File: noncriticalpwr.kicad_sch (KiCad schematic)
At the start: 6 parts, among them J4 Power Conn

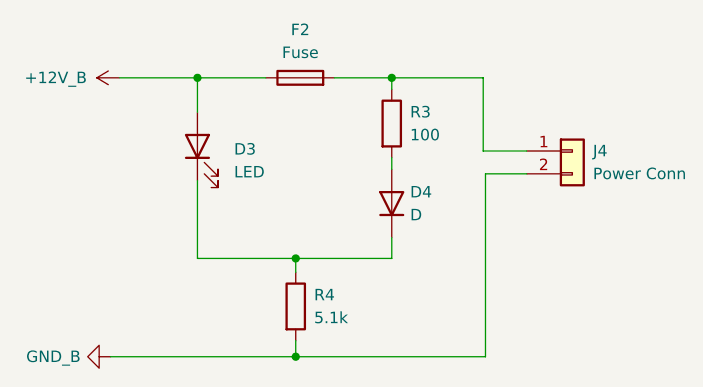
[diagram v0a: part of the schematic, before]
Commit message: removed LEDs
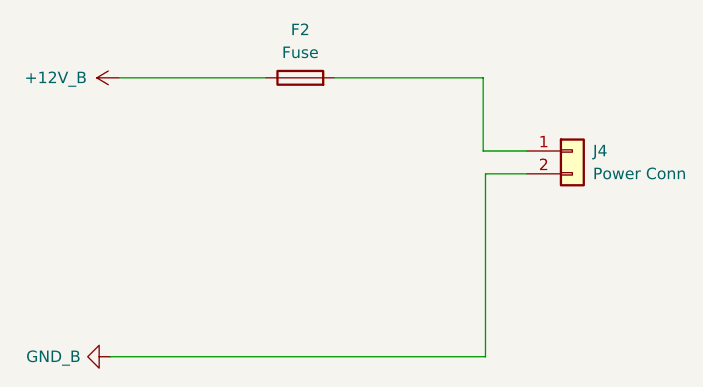
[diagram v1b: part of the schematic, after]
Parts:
- removed D3: LED, symbol Device:LED
- removed D4: D, symbol Device:D
- removed R3: 100, symbol Device:R
- removed R4: 5.1k, symbol Device:R

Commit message: finished schematic
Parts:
- added D10, D11, D12, D13, D14, D15, D16, D17, D18, D19, D8, D9: 20mA, LED_SMD:LED_0805_2012Metric, symbol Device:LED
- added F10, F11, F12, F13, F14, F15, F16, F17, F18, F19, F20: 10A, footprints:3588, symbol Device:Fuse
- added J1, J12, J13, J14, J15, J16, J17, J18, J19, J2, J20: NON CRIT OUT, footprints:Molex_Micro-Fit_3.0_43650-0215_1x02_P3.00mm_Vertical, symbol Connector_Generic:Conn_01x02
- added R10, R11, R12, R13, R14, R15, R16, R17, R18, R19, R8, R9: 505, Resistor_SMD:R_0805_2012Metric, symbol Device:R
- F2: value Fuse -> 10A
- J4: value Power Conn -> NON CRIT OUT
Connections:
- net at F2.2: now also J1.1 (Pin_1), R8.1; no longer J4.1 (Pin_1)
- net +12V_B renamed +12V_NON
- net +12V_NON: now also F10.1, F11.1, F12.1, F13.1, F14.1, F15.1, F16.1, F17.1, F18.1, F19.1, F20.1
- net GND_B renamed GND
- net GND: now also D10.1 (K), D11.1 (K), D12.1 (K), D13.1 (K), D14.1 (K), D15.1 (K), D16.1 (K), D17.1 (K), D18.1 (K), D19.1 (K), D8.1 (K), D9.1 (K), J1.2 (Pin_2), J12.2 (Pin_2), J13.2 (Pin_2), J14.2 (Pin_2), J15.2 (Pin_2), J16.2 (Pin_2), J17.2 (Pin_2), J18.2 (Pin_2), J19.2 (Pin_2), J2.2 (Pin_2), J20.2 (Pin_2)
- new net: F13.2, J13.1 (Pin_1), R12.1
- new net: D13.2 (A), R13.2
- new net: F14.2, J14.1 (Pin_1), R13.1
- new net: F20.2, J20.1 (Pin_1), R19.1
- new net: F12.2, J12.1 (Pin_1), R11.1
- new net: F10.2, J2.1 (Pin_1), R9.1
- new net: D19.2 (A), R19.2
- new net: D17.2 (A), R17.2
- new net: F19.2, J19.1 (Pin_1), R18.1
- new net: F15.2, J15.1 (Pin_1), R14.1
- new net: D15.2 (A), R15.2
- new net: D11.2 (A), R11.2
- new net: F16.2, J16.1 (Pin_1), R15.1
- new net: D8.2 (A), R8.2
- new net: F17.2, J17.1 (Pin_1), R16.1
- new net: D16.2 (A), R16.2
- new net: D14.2 (A), R14.2
- new net: D18.2 (A), R18.2
- new net: D12.2 (A), R12.2
- new net: F11.2, J4.1 (Pin_1), R10.1
- new net: D10.2 (A), R10.2
- new net: D9.2 (A), R9.2
- new net: F18.2, J18.1 (Pin_1), R17.1

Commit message: finished pcb
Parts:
- R10, R11, R12, R13, R14, R15, R16, R17, R18, R19, R8, R9: value 505 -> 1k
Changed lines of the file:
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@@
 			)
 		)
-		(property "Value" "505"
+		(property "Value" "1k"
 			(at 115.57 131.826 90)
 			(effects
@@
 			)
 		)
-		(property "Value" "505"
+		(property "Value" "1k"
 			(at 55.88 81.026 90)
 			(effects
@@
 			)
 		)
-		(property "Value" "505"
+		(property "Value" "1k"
 			(at 55.88 133.096 90)
 			(effects
@@
 			)
 		)
-		(property "Value" "505"
+		(property "Value" "1k"
 			(at 115.57 159.766 90)
 			(effects
@@
 			)
 		)
-		(property "Value" "505"
+		(property "Value" "1k"
 			(at 116.84 53.086 90)
 			(effects
@@
 			)
 		)
-		(property "Value" "505"
+		(property "Value" "1k"
 			(at 55.88 107.696 90)
 			(effects
@@
 			)
 		)
-		(property "Value" "505"
+		(property "Value" "1k"
 			(at 116.84 27.686 90)
 			(effects
@@
 			)
 		)
-		(property "Value" "505"
+		(property "Value" "1k"
 			(at 55.88 53.086 90)
 			(effects
@@
 			)
 		)
-		(property "Value" "505"
+		(property "Value" "1k"
 			(at 116.84 81.026 90)
 			(effects
@@
 			)
 		)
-		(property "Value" "505"
+		(property "Value" "1k"
 			(at 55.88 27.686 90)
 			(effects
@@
 			)
 		)
-		(property "Value" "505"
+		(property "Value" "1k"
 			(at 116.84 106.426 90)
 			(effects
@@
 			)
 		)
-		(property "Value" "505"
+		(property "Value" "1k"
 			(at 55.88 159.766 90)
 			(effects

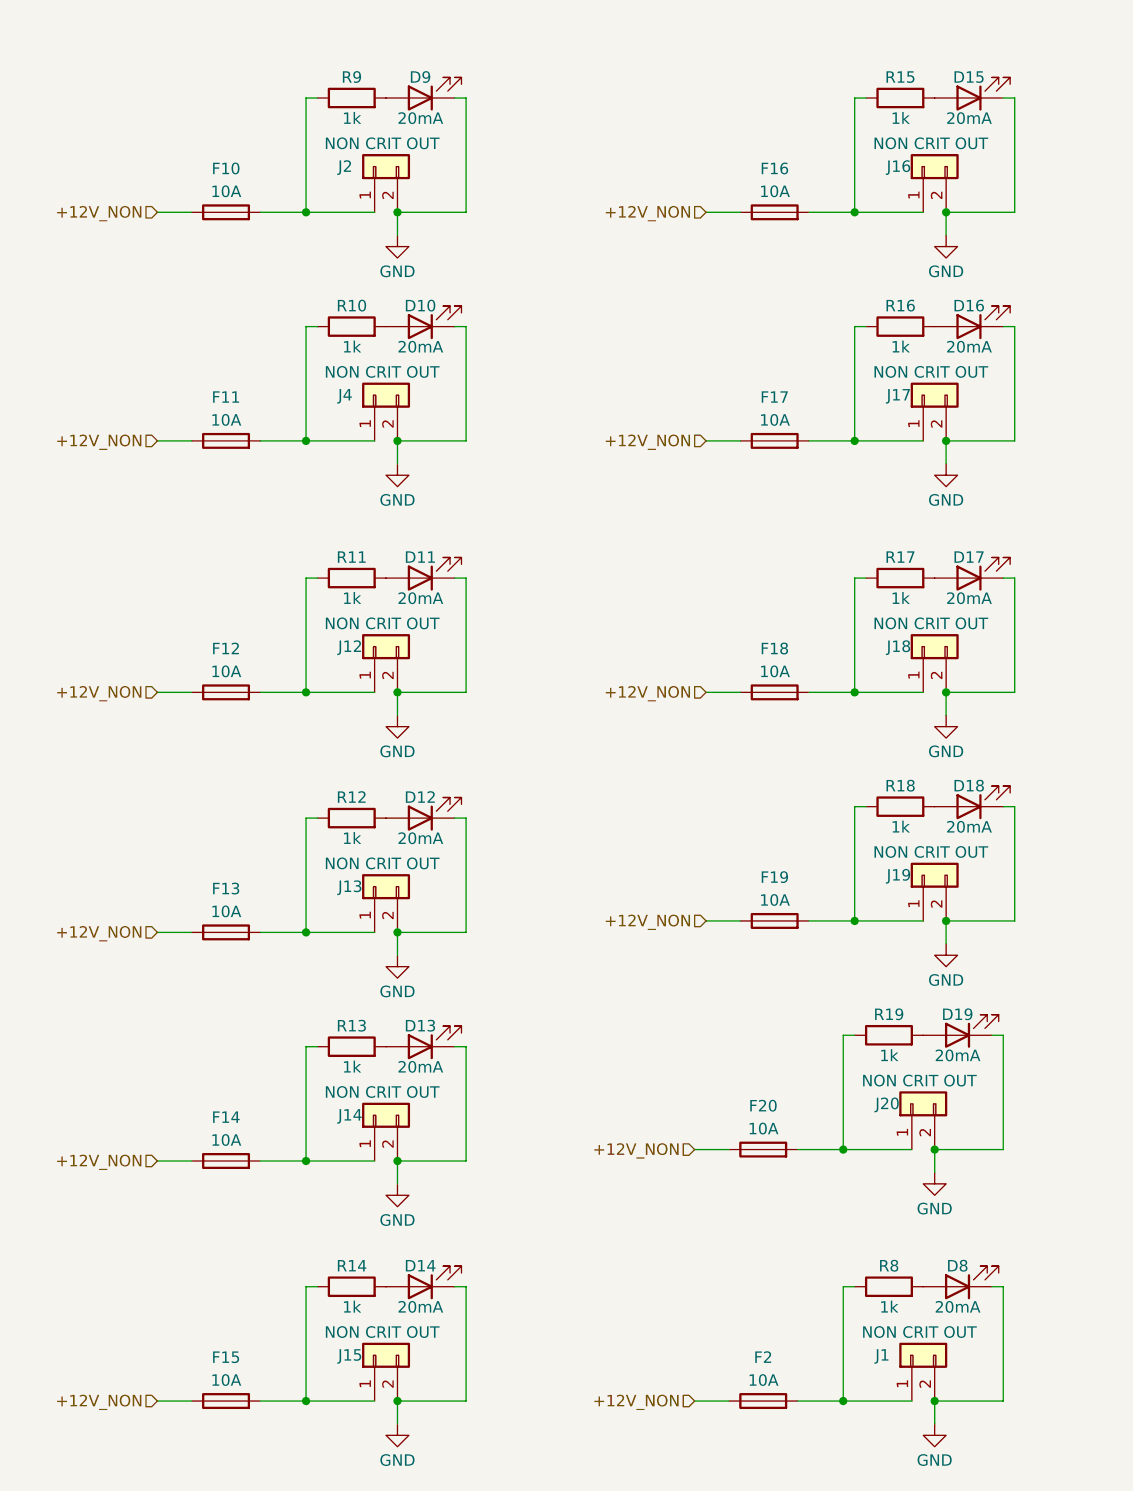
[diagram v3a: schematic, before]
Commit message: rearranged fuses on the back and and connectors on the front for improved waterproofing
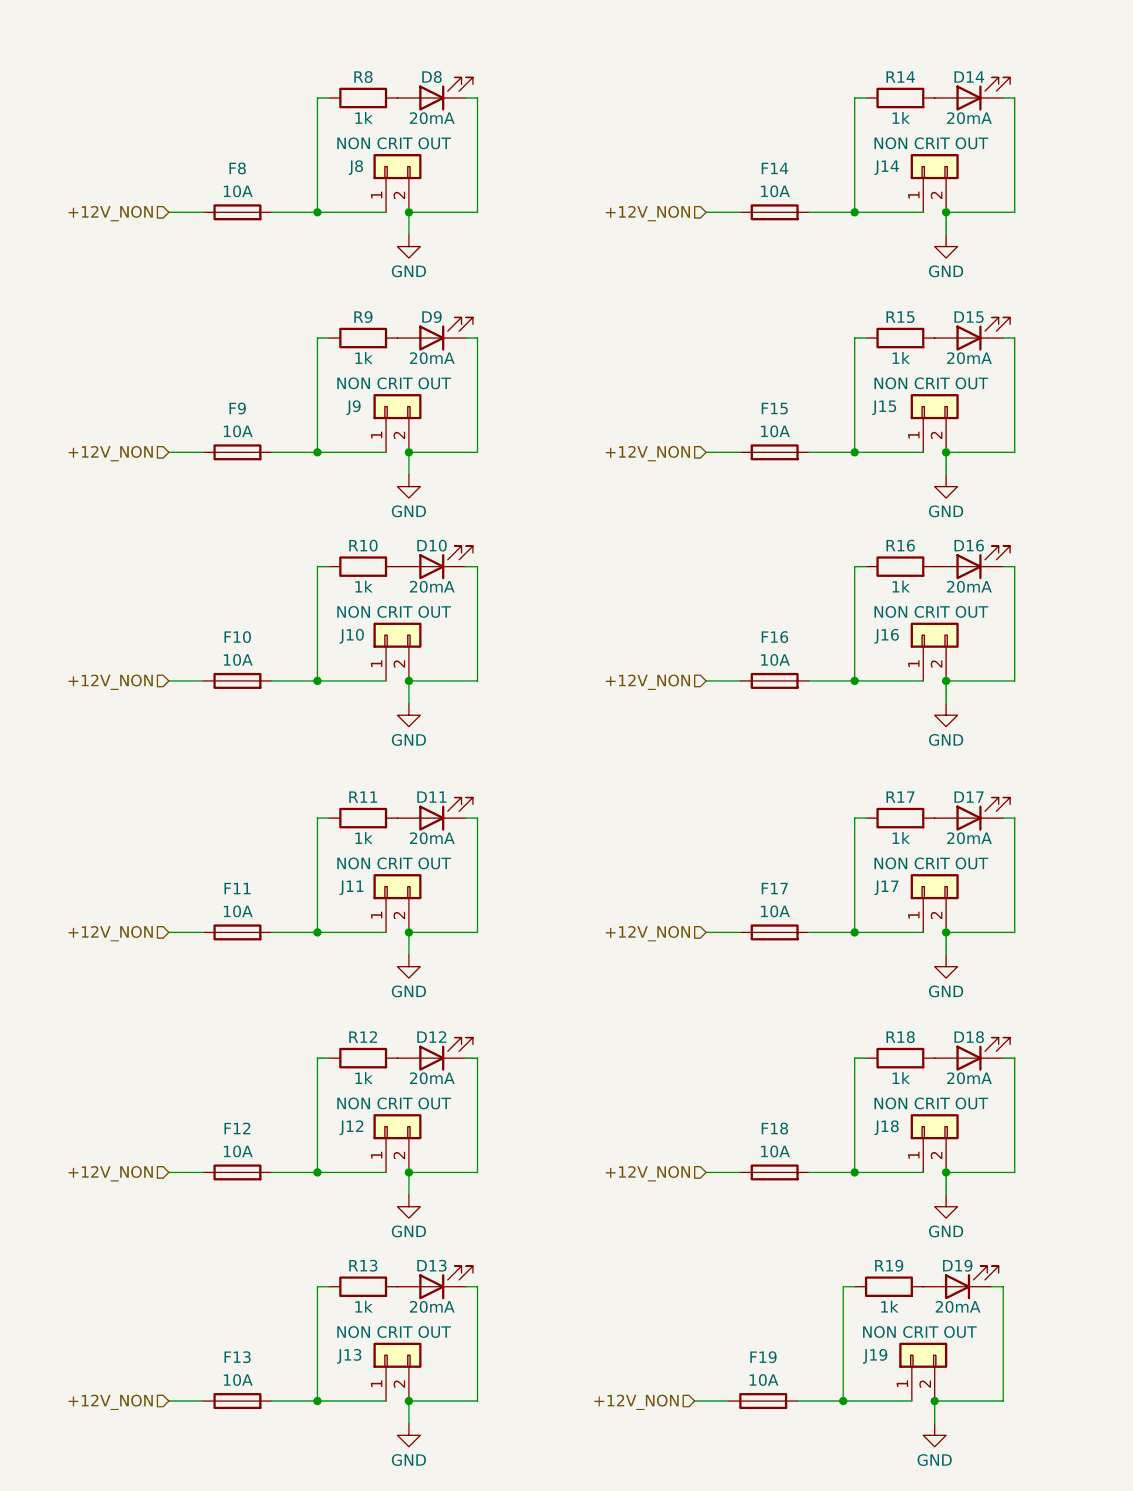
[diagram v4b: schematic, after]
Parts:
- renumbered F11 to F10, F12 to F11, F13 to F12, F14 to F13, F15 to F14, F16 to F15, F17 to F16, F18 to F17, F19 to F18, F20 to F19, F2 to F8, F10 to F9, J4 to J10, J12 to J11, J13 to J12, J14 to J13, J15 to J14, J16 to J15, J17 to J16, J18 to J17, J19 to J18, J20 to J19, J1 to J8, J2 to J9
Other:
- moved on the sheet: D10, D11, D12, D13, D14, D15, D16, D17, D18, D19, D8, D9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

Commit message: reoriented fuses horizontally to fit enclosure dimensions
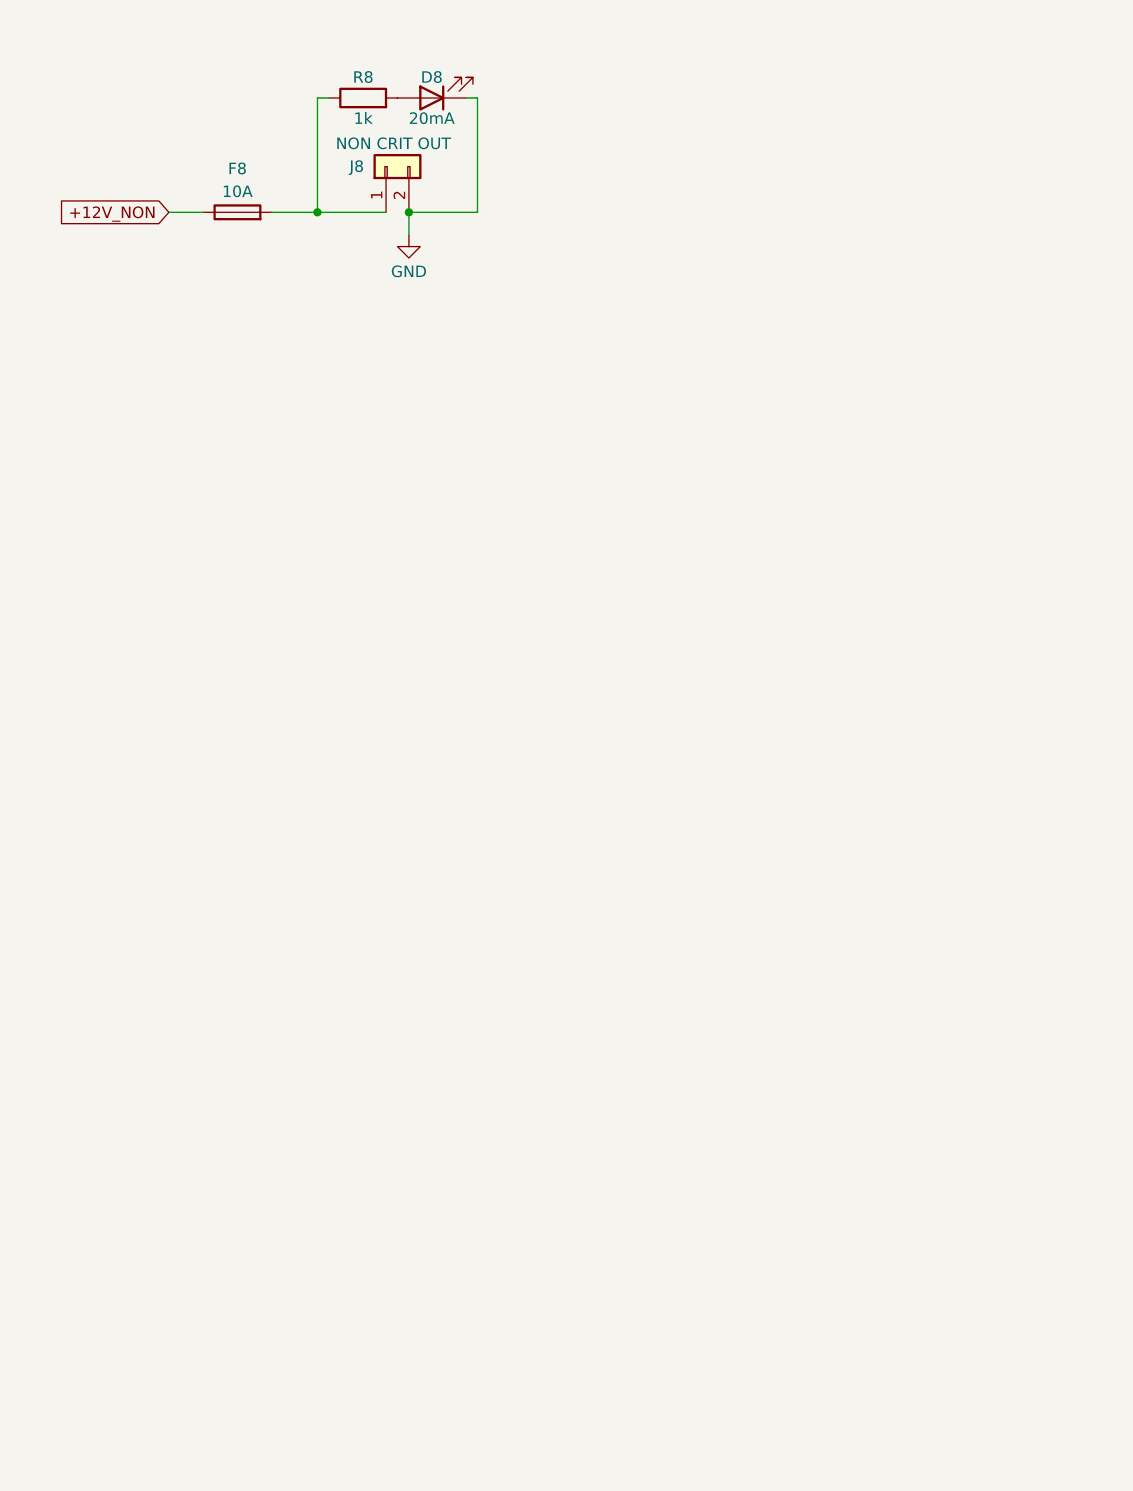
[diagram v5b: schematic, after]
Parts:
- removed D10, D11, D12, D13, D14, D15, D16, D17, D18, D19, D9: 20mA, LED_SMD:LED_0805_2012Metric, symbol Device:LED
- removed F10, F11, F12, F13, F14, F15, F16, F17, F18, F19, F9: 10A, footprints:3588, symbol Device:Fuse
- removed J10, J11, J12, J13, J14, J15, J16, J17, J18, J19, J9: NON CRIT OUT, footprints:Molex_Micro-Fit_3.0_43650-0215_1x02_P3.00mm_Vertical, symbol Connector_Generic:Conn_01x02
- removed R10, R11, R12, R13, R14, R15, R16, R17, R18, R19, R9: 1k, Resistor_SMD:R_0805_2012Metric, symbol Device:R

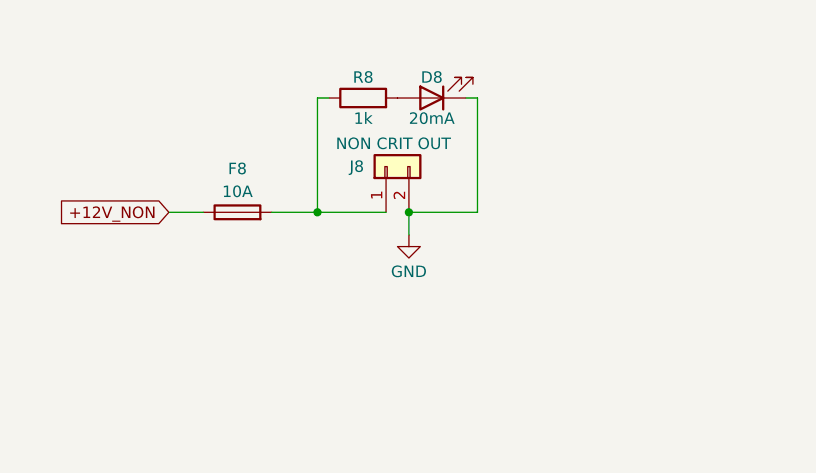
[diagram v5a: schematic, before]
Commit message: Added optoisolators to ensure LED indicators are powered by critical power and only turn on when the fuse blows. Fuses and resistors on the back for waterproofing.
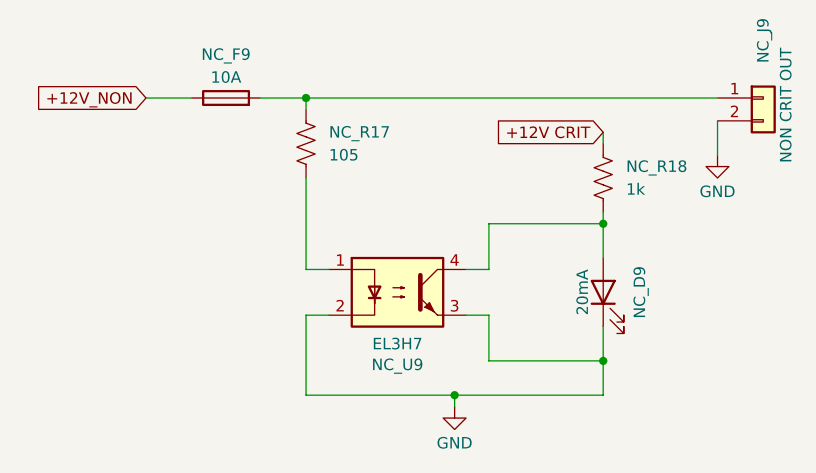
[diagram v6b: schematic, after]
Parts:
- removed D8: 20mA, LED_SMD:LED_0805_2012Metric, symbol Device:LED
- removed F8: 10A, footprints:3588, symbol Device:Fuse
- removed J8: NON CRIT OUT, footprints:Molex_Micro-Fit_3.0_43650-0215_1x02_P3.00mm_Vertical, symbol Connector_Generic:Conn_01x02
- removed R8: 1k, Resistor_SMD:R_0805_2012Metric, symbol Device:R
- added NC_D9: 20mA, LED_SMD:LED_0805_2012Metric, symbol Device:LED
- added NC_F9: 10A, footprints:3588, symbol Device:Fuse
- added NC_J9: NON CRIT OUT, footprints:Molex_Micro-Fit_3.0_43650-0215_1x02_P3.00mm_Vertical, symbol Connector_Generic:Conn_01x02
- added NC_R17: 105, Resistor_SMD:R_0805_2012Metric, symbol Device:R_US
- added NC_R18: 1k, Resistor_SMD:R_0805_2012Metric, symbol Device:R_US
- added NC_U9: EL3H7, Package_SO:SOP-4_4.4x2.6mm_P1.27mm, symbol Isolator:SFH617A-1
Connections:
- net +12V_NON: now also NC_F9.1
- net GND: now also NC_D9.1 (K), NC_J9.2 (Pin_2), NC_U9.2, NC_U9.3
- new net: NC_D9.2 (A), NC_R18.2, NC_U9.4
- new net: NC_F9.2, NC_J9.1 (Pin_1), NC_R17.1
- new net: NC_R17.2, NC_U9.1
- new net +12V CRIT: NC_R18.1
